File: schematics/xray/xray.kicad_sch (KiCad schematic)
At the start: 103 parts, among them J1 USB_A, J2 USB_B_Micro, J3 USB_C_Receptacle_USB2.0, J4 USBASP, M1 VibroMotor, 3V, 8x2.7mm, Q1 IRF7413ZPbF, Q10 IRLML0030, Q11 IRLML0030, Q2 IRF7424PBF, Q3 IRLML0030, Q4 IRF7424PBF, Q5 IRLML0030, Q6 BC857, Q7 BC847, Q8 IRLML0030, Q9 IRLML0030, SW1 EC11W****, T1 Transformer_1P_1S, U1 IP5328P, U2 ATmega328P-A, U3 SN74LVC2T45DCUR, U4 SN74LVC2T45DCUR, U5 SN74LVC2T45DCUR, U6 Display_1.18inch_st7535, Y1 HC-49SM, 8MHz

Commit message: debugging...
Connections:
- net FLASHLIGHT: now also U2.9 (PD5); no longer U2.14 (PB2)
- net SPEAKER: now also U2.14 (PB2); no longer U2.13 (PB1)
- net USB_INT: now also U2.13 (PB1); no longer U2.9 (PD5)

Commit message: continue working under firmware and schematics
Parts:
- added C39: 100 nF, Capacitor_SMD:C_0603_1608Metric, symbol Device:C
- added C7: 200 pF, Capacitor_SMD:C_1206_3216Metric, symbol Device:C
- added R23: 1M, Resistor_SMD:R_0805_2012Metric, symbol Device:R
- added R25: RSET [?], Resistor_SMD:R_0805_2012Metric, symbol Device:R
- added R7: 200K, Resistor_SMD:R_0805_2012Metric, symbol Device:R
- added SW2: B3F3150, Button_Switch_THT:SW_Tactile_SKHH_Angled, symbol Switch:SW_DIP_x01
- added U1: PCA9306, Package_SO:MSOP-8_3x3mm_P0.65mm, symbol Interface:PCA9306
- BT1: value Li-Ion, 3.7V, 10000 mAh, 1260100 -> Li-Ion, 4.2V, 10000 mAh, 1260100
- renumbered C7 to C10, C14 to C11, C8 to C12, C9 to C13, C18 to C14, C11 to C15, C12 to C16, C15 to C18, C16 to C19, C24 to C20, C19 to C21, C20 to C22, C21 to C23, C23 to C24, C22 to C25, C25 to C26, C26 to C27, C29 to C28, C27 to C29, C33 to C32, C28 to C33, C32 to C34, C34 to C35, C35 to C36, C36 to C37, C37 to C38, C10 to C8, C13 to C9, Q6 to Q5, Q5 to Q6, R5 to R10, R6 to R11, R9 to R12, R10 to R13, R12 to R14, R16 to R15, R11 to R16, R13 to R17, R20 to R2, R14 to R20, R15 to R21, R17 to R22, R22 to R24, R23 to R26, R24 to R27, R25 to R28, R26 to R29, R21 to R3, R27 to R30, R2 to R4, R3 to R5, R4 to R6, R7 to R8, R8 to R9, U1 to U2, U2 to U3, U3 to U4, U4 to U5, U5 to U6, U6 to U7
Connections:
- net GND: now also C39.1, C7.1, R23.2, R25.2, SW2.2, U1.1 (GND)
- net USB_FORCE_ON: now also U3.19 (ADC6), R23.1; no longer U3.11 (PD7)
- net USB_INT: now also R25.1
- net VREG: now also U1.2 (VREF1)
- net USB_I2C_ENABLE: now reaches U3.22 (ADC7)
- net USB_I2C_ENABLE: now also R7.1
- net I2C_SCL renamed USB_I2C_SCL
- net USB_I2C_SCL: now also U1.3 (SCL1); no longer U3.28 (PC5)
- net I2C_SDA renamed USB_I2C_SDA
- net USB_I2C_SDA: now also U1.4 (SDA1); no longer U3.27 (PC4)
- new net: C7.2, R7.2, U1.7 (VREF2), U1.8 (EN)
- new net MCU_I2C_SCL: U1.6 (SCL2), U3.28 (PC5)
- new net MCU_I2C_SDA: U1.5 (SDA2), U3.27 (PC4)
- new net WAKEUP_BUTTON: C39.2, SW2.1, U3.11 (PD7)
- no-connect marks 12 -> 10
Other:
- note added: "NOTE [?] You can use this R to reduce max volume. Use 0 ohm for max volume"
- note added: "NOTE [RSET?] Not installed for VCC=4.2V But in another datasheet I see something like 510K"
- note removed: "NOTE [?] You can use this R to reduce volume. Use 0 ohm for max volume"
- moved on the sheet: BT1, C10, C12, C13, C14, C15, C16, C17, C18, C19, C21, C22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

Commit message: fixed display schematics
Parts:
- removed Q9: IRLML0030, Package_TO_SOT_SMD:SOT-23, symbol Transistor_FET:IRLML0030
- added Q9: IRLML5203, Package_TO_SOT_SMD:SOT-23, symbol Transistor_FET:IRLML5203
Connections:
- net GND: now also U7.10 (GND), U7.9 (GND); no longer R27.1
- net USB_FORCE_ON: now also U3.25 (PC2); no longer U3.19 (ADC6)
- net VCC: now also R27.2, R7.1, Q9.2 (S); no longer U7.11 (VCC)
- net TFT_ENABLE renamed TFT_ENABLE#
- net TFT_ENABLE#: now also R27.1, Q9.1 (G); no longer R27.2
- net TFT_RESET: no longer names the net of U7.2 (RESET)
- net TFT_RESET: now also U7.11 (VCC), Q9.3 (D); no longer U3.25 (PC2)
- net USB_I2C_ENABLE: no longer names the net of U3.22 (ADC7)
- net USB_I2C_ENABLE: no longer R7.1
- no-connect marks 10 -> 12
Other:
- note added: "ERROR Wrong freq: 12.5KHz, expected 500Hz"
- note added: "ERROR no PWM on hardware"
- moved on the sheet: U7

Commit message: continue working under schematics and firmware
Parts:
- added C40: 100 uF, Capacitor_THT:CP_Radial_D5.0mm_P2.50mm, symbol Device:C_Polarized
- added Q11, Q14: IRLML0030, Package_TO_SOT_SMD:SOT-23, symbol Transistor_FET:IRLML0030
- added Q9: IRLML5203, Package_TO_SOT_SMD:SOT-23, symbol Transistor_FET:IRLML5203
- added R27: 10K, Resistor_SMD:R_0805_2012Metric, symbol Device:R
- added R28, R32: 200K, Resistor_SMD:R_0805_2012Metric, symbol Device:R
- R23, R26, R4: value 1M -> 200K
- R29: renamed from R27; value 1M -> 200K
- R31: renamed from R29; value 1M -> 200K
- R33: renamed from R30; value 1M -> 200K
- renumbered C39 to C38, C38 to C39, Q9 to Q10, Q10 to Q12, Q11 to Q13, R28 to R30
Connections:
- net GND: now also C40.2, Q11.2 (S), Q14.2 (S)
- net RESET: now also Q14.3 (D)
- net VCC: now also Q9.2 (S), R27.2
- net WAKEUP_BUTTON: now also Q11.1 (G), Q9.1 (G), R27.1
- new net: R28.1, R32.2
- new net: Q9.3 (D), R28.2
- new net: C40.1, Q11.3 (D), Q14.1 (G), R32.1
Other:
- note added: "NOTE* [TASK] 1. I have to find frequency to work on. At now avaiable variants: 1.1 82Khz [requires capacity ~ 7nF] 1.2 100Khz [requires capacity ~ 21nF]"
- note added: "TODO: check reset on hardware"
- note removed: "ERROR Wrong freq: 12.5KHz, expected 500Hz"
- note removed: "ERROR no PWM on hardware"
- note removed: "NOTE* [TASK] 1. I have to check mosfet to work here 2. I have to find frequency to work on. At now avaiable variants: 2.1 82Khz [requires capacity ~ 7nF] 2.2 100Khz [requires capacity ~ 21nF]"
- moved on the sheet: BT1, C38, Q10, R29, SW2, U7

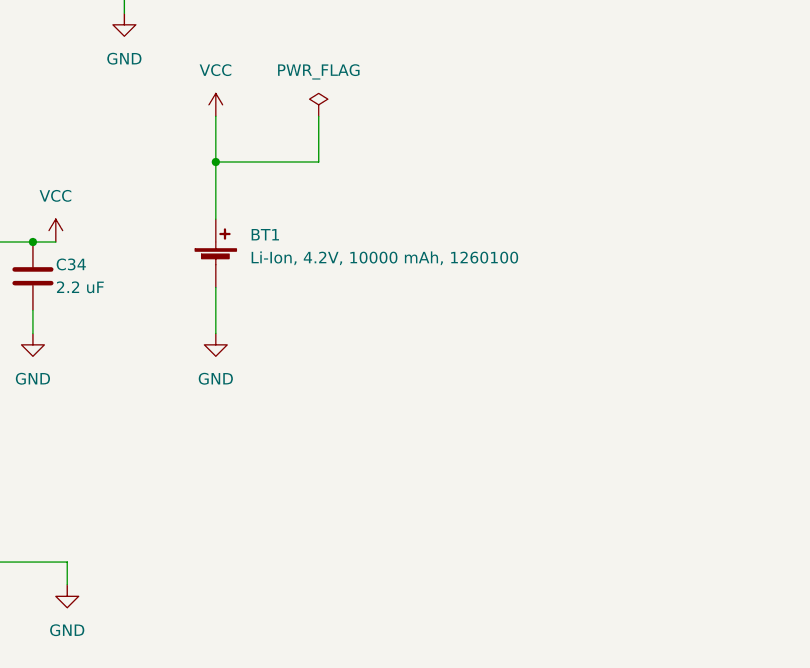
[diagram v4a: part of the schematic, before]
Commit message: added fuse to vbat
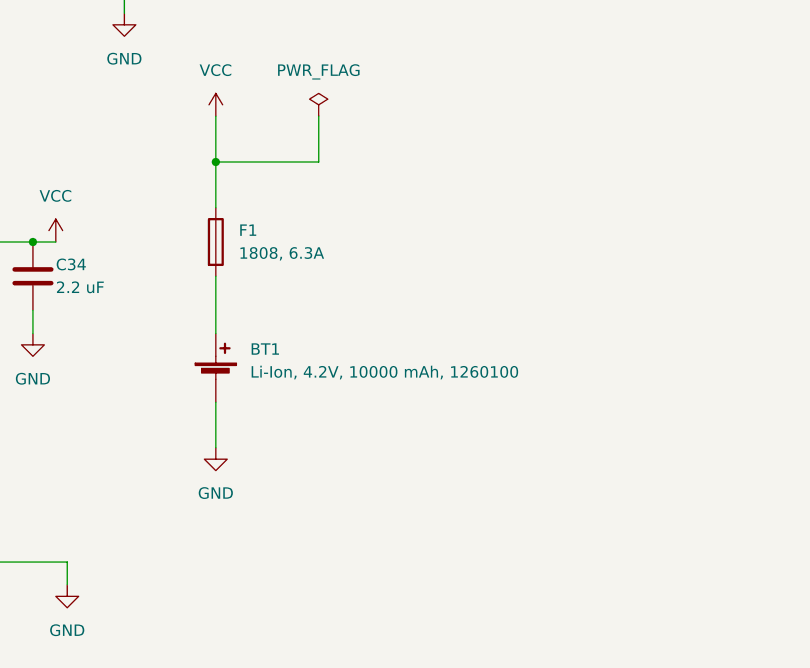
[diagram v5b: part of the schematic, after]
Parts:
- added F1: 1808, 6.3A, Library:FuseHolder1808, symbol Device:Fuse
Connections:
- net VCC: now also F1.1; no longer BT1.1 (+)
- new net: BT1.1 (+), F1.2
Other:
- moved on the sheet: BT1
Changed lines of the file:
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@@
   (junction (at 196.85 166.37) (diameter 0) (color 0 0 0 0)
   )
+  (junction (at 328.93 49.53) (diameter 0) (color 0 0 0 0)
+  )
   (junction (at 530.86 99.06) (diameter 0) (color 0 0 0 0)
   )
@@
   (junction (at 525.78 223.52) (diameter 0) (color 0 0 0 0)
   )
-  (junction (at 328.93 49.53) (diameter 0) (color 0 0 0 0)
-  )
   (junction (at 265.43 222.25) (diameter 0) (color 0 0 0 0)
   )
@@
     (stroke (width 0) (type default) (color 0 0 0 0))
   )
-  (wire (pts (xy 328.93 49.53) (xy 328.93 55.88))
-    (stroke (width 0) (type default) (color 0 0 0 0))
-  )
   (wire (pts (xy 359.41 199.39) (xy 336.55 199.39))
     (stroke (width 0) (type default) (color 0 0 0 0))
@@
     (stroke (width 0) (type default) (color 0 0 0 0))
   )
+  (wire (pts (xy 328.93 49.53) (xy 328.93 54.61))
+    (stroke (width 0) (type default) (color 0 0 0 0))
+  )
   (wire (pts (xy 31.75 104.14) (xy 35.56 104.14))
     (stroke (width 0) (type default) (color 0 0 0 0))
@@
     (stroke (width 0) (type default) (color 0 0 0 0))
   )
-  (wire (pts (xy 328.93 63.5) (xy 328.93 68.58))
+  (wire (pts (xy 328.93 76.2) (xy 328.93 81.28))
     (stroke (width 0) (type default) (color 0 0 0 0))
   )
@@
     (stroke (width 0) (type default) (color 0 0 0 0))
   )
+  (wire (pts (xy 328.93 62.23) (xy 328.93 68.58))
+    (stroke (width 0) (type default) (color 0 0 0 0))
+  )
   (wire (pts (xy 326.39 165.1) (xy 326.39 168.91))
     (stroke (width 0) (type default) (color 0 0 0 0))
@@
     (pin "2")
   )
-  (symbol (lib_id "power:GND") (at 328.93 68.58 0) (unit 1)
+  (symbol (lib_id "power:GND") (at 328.93 81.28 0) (unit 1)
     (in_bom yes) (on_board yes) (fields_autoplaced)
-    (property "Reference" "#PWR049" (id 0) (at 328.93 74.93 0)
+    (property "Reference" "#PWR049" (id 0) (at 328.93 87.63 0)
       (effects (font (size 1.27 1.27)) hide)
     )
-    (property "Value" "GND" (id 1) (at 328.93 73.66 0))
-    (property "Footprint" "" (id 2) (at 328.93 68.58 0)
+    (property "Value" "GND" (id 1) (at 328.93 86.36 0))
+    (property "Footprint" "" (id 2) (at 328.93 81.28 0)
       (effects (font (size 1.27 1.27)) hide)
     )
-    (property "Datasheet" "" (id 3) (at 328.93 68.58 0)
+    (property "Datasheet" "" (id 3) (at 328.93 81.28 0)
       (effects (font (size 1.27 1.27)) hide)
     )
@@
     (pin "2")
   )
+  (symbol (lib_id "Device:Fuse") (at 328.93 58.42 0) (unit 1)
+    (in_bom yes) (on_board yes) (fields_autoplaced)
+    (property "Reference" "F1" (id 0) (at 331.47 57.1499 0)
+      (effects (font (size 1.27 1.27)) (justify left))
+    )
+    (property "Value" "1808, 6.3A" (id 1) (at 331.47 59.6899 0)
+      (effects (font (size 1.27 1.27)) (justify left))
+    )
+    (property "Footprint" "Library:FuseHolder1808" (id 2) (at 327.152 58.42 90)
+      (effects (font (size 1.27 1.27)) hide)
+    )
+    (property "Datasheet" "~" (id 3) (at 328.93 58.42 0)
+      (effects (font (size 1.27 1.27)) hide)
+    )
+    (pin "1")
+    (pin "2")
+  )
   (symbol (lib_id "power:+5V") (at 377.19 194.31 0) (unit 1)
     (in_bom yes) (on_board yes) (fields_autoplaced)
@@
     (pin "1")
   )
-  (symbol (lib_id "Device:Battery_Cell") (at 328.93 60.96 0) (unit 1)
+  (symbol (lib_id "Device:Battery_Cell") (at 328.93 73.66 0) (unit 1)
     (in_bom yes) (on_board yes)
-    (property "Reference" "BT1" (id 0) (at 332.74 57.6579 0)
+    (property "Reference" "BT1" (id 0) (at 332.74 70.3579 0)
       (effects (font (size 1.27 1.27)) (justify left))
     )
-    (property "Value" "Li-Ion, 4.2V, 10000 mAh, 1260100" (id 1) (at 332.74 60.1979 0)
+    (property "Value" "Li-Ion, 4.2V, 10000 mAh, 1260100" (id 1) (at 332.74 72.8979 0)
       (effects (font (size 1.27 1.27)) (justify left))
     )
-    (property "Footprint" "Connector_Wire:SolderWire-0.15sqmm_1x02_P4mm_D0.5mm_OD1.5mm" (id 2) (at 328.93 59.436 90)
+    (property "Footprint" "Connector_Wire:SolderWire-0.15sqmm_1x02_P4mm_D0.5mm_OD1.5mm" (id 2) (at 328.93 72.136 90)
       (effects (font (size 1.27 1.27)) hide)
     )
-    (property "Datasheet" "~" (id 3) (at 328.93 59.436 90)
+    (property "Datasheet" "~" (id 3) (at 328.93 72.136 90)
       (effects (font (size 1.27 1.27)) hide)
     )
@@
       (reference "D6") (unit 1) (value "FLASH") (footprint "Connector_Wire:SolderWire-0.5sqmm_1x02_P4.6mm_D0.9mm_OD2.1mm")
     )
+    (path "/807aff56-2132-47e6-b95e-f5b9f73ab31a"
+      (reference "F1") (unit 1) (value "1808, 6.3A") (footprint "Library:FuseHolder1808")
+    )
     (path "/448c05ee-1a3b-4e6c-ae1a-382f2aa70f20"

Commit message: board production started
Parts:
- removed L1: 10 uH, Capacitor_SMD:C_1210_3225Metric, symbol Device:L
- removed R32: 200K, Resistor_SMD:R_0805_2012Metric, symbol Device:R
- added H1, H3: MountingHole, MountingHole:MountingHole_3.2mm_M3, symbol Mechanical:MountingHole
- added JP1: SolderJumper_2_Open, Jumper:SolderJumper-2_P1.3mm_Open_TrianglePad1.0x1.5mm, symbol Jumper:SolderJumper_2_Open
- added R26, R28, R29: 0, Resistor_SMD:R_1206_3216Metric, symbol Device:R
- C11, C8, C9: value 0.1 uF, 630V -> К73-17, 0.1 uF, 630V
- C23: renamed from C24; value 100 nF -> 470 nF
- C24: renamed from C20; value ~10 pF, 630V -> CC81, 10 pF, 630V
- C30, C31, C5, C7: footprint Capacitor_SMD:C_1206_3216Metric -> Capacitor_SMD:C_0603_1608Metric
- C32: renamed from C33; footprint Capacitor_SMD:C_1206_3216Metric -> Capacitor_SMD:C_0603_1608Metric
- C33: renamed from C34; footprint Capacitor_SMD:C_1206_3216Metric -> Capacitor_SMD:C_0603_1608Metric
- C34: renamed from C32; footprint Capacitor_SMD:C_1206_3216Metric -> Capacitor_SMD:C_0603_1608Metric
- C6: value see note LC* -> see note [*]; footprint Capacitor_SMD:C_1206_3216Metric -> Capacitor_SMD:C_0603_1608Metric
- D3: footprint Diode_SMD:D_SMA -> Diode_THT:D_5W_P5.08mm_Vertical_AnodeUp
- F1: value 1808, 6.3A -> 1808, 6A
- L2: renamed from L3; value 10 uH -> 20 uH; footprint Capacitor_SMD:C_1210_3225Metric -> Inductor_SMD:L_1210_3225Metric
- Q1: value IRF7413ZPbF -> IRF7832PbF
- Q2, Q4: value IRF7424PBF -> IRF7425PbF; footprint Package_SO:SO-8_3.9x4.9mm_P1.27mm -> Package_SO:SOIC-8_3.9x4.9mm_P1.27mm
- R16: renamed from R17; footprint Resistor_SMD:R_0805_2012Metric -> Resistor_SMD:R_1206_3216Metric
- R17: renamed from R15; value 200K** (82K ?) -> 67K**
- R24: renamed from R25; value RSET [?] -> VSET [?]
- R31: renamed from R28; value 200K -> 400K
- R33: renamed from R30; value 0 ? -> 0; footprint Resistor_SMD:R_0805_2012Metric -> Resistor_SMD:R_1206_3216Metric
- renumbered C21 to C20, C22 to C21, C23 to C22, J2 to J1, J1 to J2, JP1 to JP2, L2 to L1, R8 to R10, R9 to R11, R16 to R15, R20 to R18, R21 to R19, R22 to R20, R18 to R21, R23 to R22, R19 to R23, R24 to R25, R26 to R27, R27 to R30, R29 to R32, R31 to R34, R33 to R35, R10 to R8, R11 to R9
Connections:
- net VCC: now also R1.1, R26.2, R28.2, R29.2; no longer D4.2 (A), D5.2 (A), D6.2 (A)
- net at C11.2, D3.1 (K): now also JP1.1 (A); no longer R10.1
- net at R31.1: now also C40.1, Q11.3 (D), Q14.1 (G)
- net DCDC_L: no longer names the net of C18.2, L1.2, U2.14 (LX_1), U2.15 (LX_2), U2.16 (LX_3), U2.17 (LX_4), U2.18 (LX_5)
- new net: D6.2 (A), R29.1
- new net: JP1.2 (B), R10.1
- new net: D5.2 (A), R28.1
- new net: D4.2 (A), R26.1
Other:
- note added: "NOTE [VSET?] One datasheet says 'Not installed for VCC=4.2V' But in another version of datasheet I saw something like 510K"
- note added: "NOTE* These capacitors should be selected so that the output voltage is maximum"
- note added: "USB_VSYS & USV_VMID lines: max ~ 25V"
- note added: "You can use this R to reduce max volume. Use 0 ohm for max volume"
- note removed: "NOTE [?] You can use this R to reduce max volume. Use 0 ohm for max volume"
- note removed: "NOTE [RSET?] Not installed for VCC=4.2V But in another datasheet I see something like 510K"
- note removed: "NOTE* [TASK] 1. I have to find frequency to work on. At now avaiable variants: 1.1 82Khz [requires capacity ~ 7nF] 1.2 100Khz [requires capacity ~ 21nF]"
- moved on the sheet: C2, C24, C3, C34, D4, D5, D6, J1, J2, Q1, Q2, Q5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

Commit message: Intermediate commit before re-writing ATMega and IP5328 integration
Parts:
- C33: footprint Capacitor_SMD:C_0603_1608Metric -> 100 nF
- C34: value 200 pF*** -> 330 pF***
- J4: Spice_Model USBASP -> (none); Spice_Netlist_Enabled Y -> (none); Spice_Primitive J -> (none)
- L1: symbol pspice:INDUCTOR -> Device:L
- R24: value VSET [?] -> 510K
- R26, R29: value 0 -> 16
- R28, R33: value 0 -> 27
- R9: value 100K@25C -> NTCM-100K@25-B4250
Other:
- note added: "NOTE ** I have to find nominal of this R to reduce signal time MAX Timp = 1 / (2.5 * 10^4) = 40 mkS Expected Timp ~ 10-20mkS"
- note added: "NOTE* These capacitors used to adjust output voltage"
- note added: "NOTE*** Nmax for SBT11A == 2.5*10^4 imp/sec == 25Khz LF filter: 10K + 330pF ~ 48Khz Freq of UV source ~ 100hz"
- note added: "T1: N in [1-2] : ~18 turns (change it to adjust output voltage) N out [3-4] : 1000 turns Ferite core : М2000НМ, Ш4х4, clearance - manual ~1-2mm, adjust it. Coil frame : Ш4х4 2 x https://www.chipdip.ru/product/m2000nm-sh4x4-1-sht 1 x https://www.chipdip.ru/product/katushka-karkas-pod-sh-4x4"
- note added: "You can use this R to reduce max volume. Use 0 ohm for max volume Be carefull with max-current of your speaker"
- note removed: "NOTE ** [TASK] I have to find nominal of this R to reduce signal time MAX Timp = 1 / (2.5 * 10^4) = 40 mkS Expected Timp ~ 10-20mkS"
- note removed: "NOTE* These capacitors should be selected so that the output voltage is maximum"
- note removed: "NOTE*** Nmax for SBT11A == 2.5*10^4 imp/sec == 25Khz LF filter: 10K + 200pF ~ 80Khz Freq of UV source ~ 300Khz"
- note removed: "You can use this R to reduce max volume. Use 0 ohm for max volume"

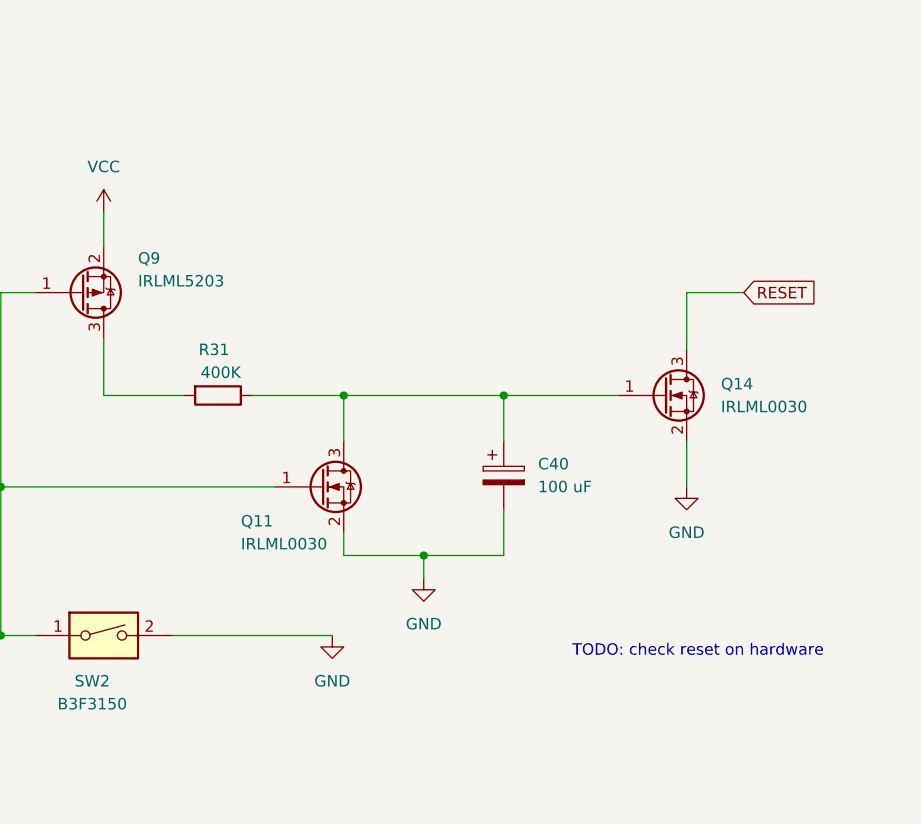
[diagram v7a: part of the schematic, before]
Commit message: Prepare to re-write UI
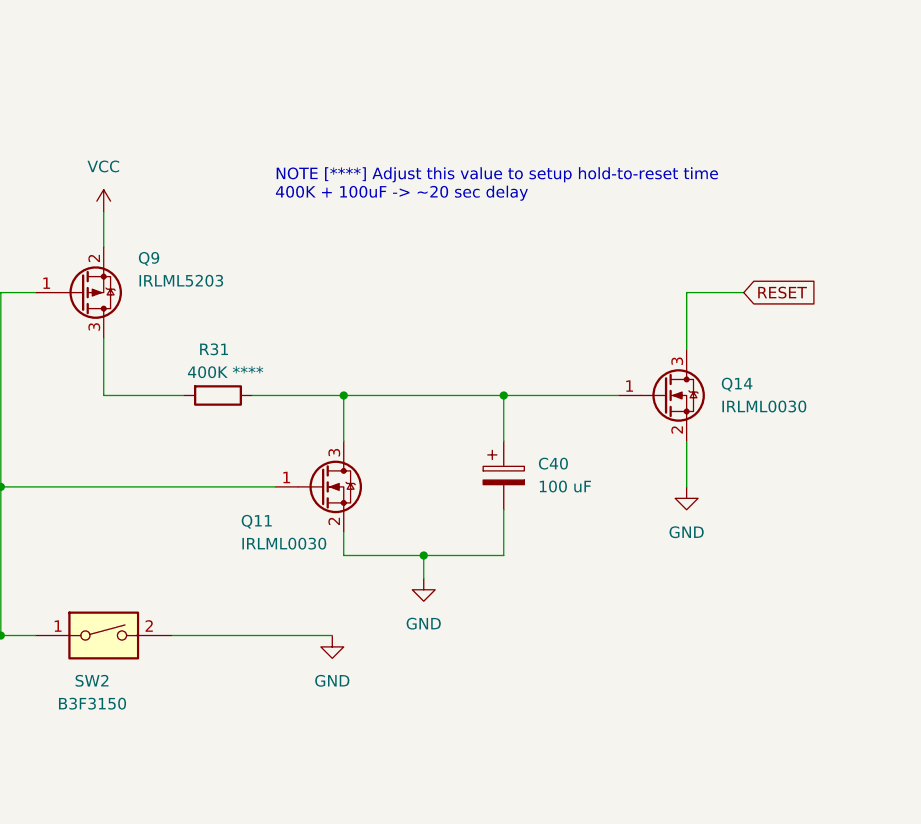
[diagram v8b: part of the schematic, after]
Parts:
- C33: footprint 100 nF -> Capacitor_SMD:C_0603_1608Metric
- R31: value 400K -> 400K ****
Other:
- note added: "NOTE [****] Adjust this value to setup hold-to-reset time 400K + 100uF -> ~20 sec delay"
- note removed: "TODO: check reset on hardware"
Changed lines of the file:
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@@
     (effects (font (size 1.27 1.27)) (justify left bottom))
   )
-  (text "TODO: check reset on hardware" (at 542.29 234.95 0)
+  (text "NOTE [****] Adjust this value to setup hold-to-reset time\n400K + 100uF -> ~20 sec delay"
+    (at 509.27 184.15 0)
     (effects (font (size 1.27 1.27)) (justify left bottom))
   )
@@
       (effects (font (size 1.27 1.27)) (justify left))
     )
-    (property "Footprint" "100 nF" (at 309.5752 66.04 0)
+    (property "Footprint" "Capacitor_SMD:C_0603_1608Metric" (at 309.5752 66.04 0)
       (effects (font (size 1.27 1.27)) hide)
     )
@@
       (effects (font (size 1.27 1.27)) (justify right))
     )
-    (property "Value" "400K" (at 505.46 203.2 90)
+    (property "Value" "400K ****" (at 508 203.2 90)
       (effects (font (size 1.27 1.27)) (justify right))
     )
